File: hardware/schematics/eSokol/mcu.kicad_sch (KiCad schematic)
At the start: 14 parts, among them J1 DB25, Q6 AO3400A, SW1 SW_LITTLE, U2 YAAJ_BluePill_SWD_Breakout, U3 TP4056, U5 AMS1117-5.0, U9 TCRT5000

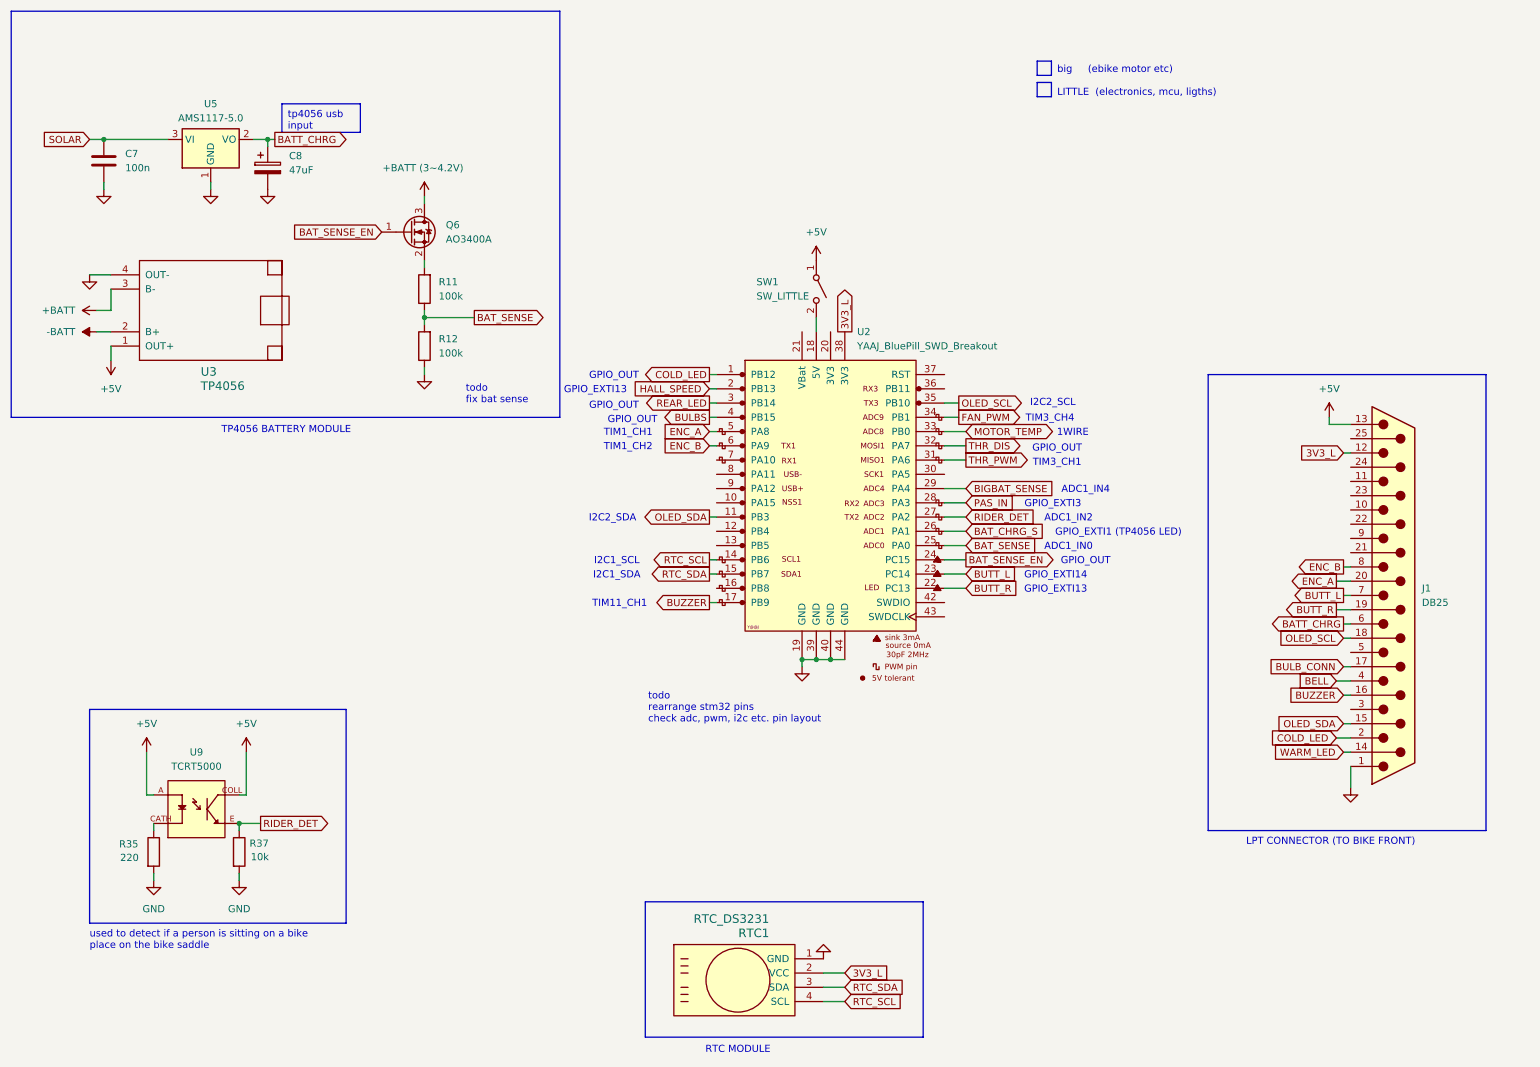
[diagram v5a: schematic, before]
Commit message: Minor lights fixes and improvements, added decoupling cap to mcu 5V, removed unused files
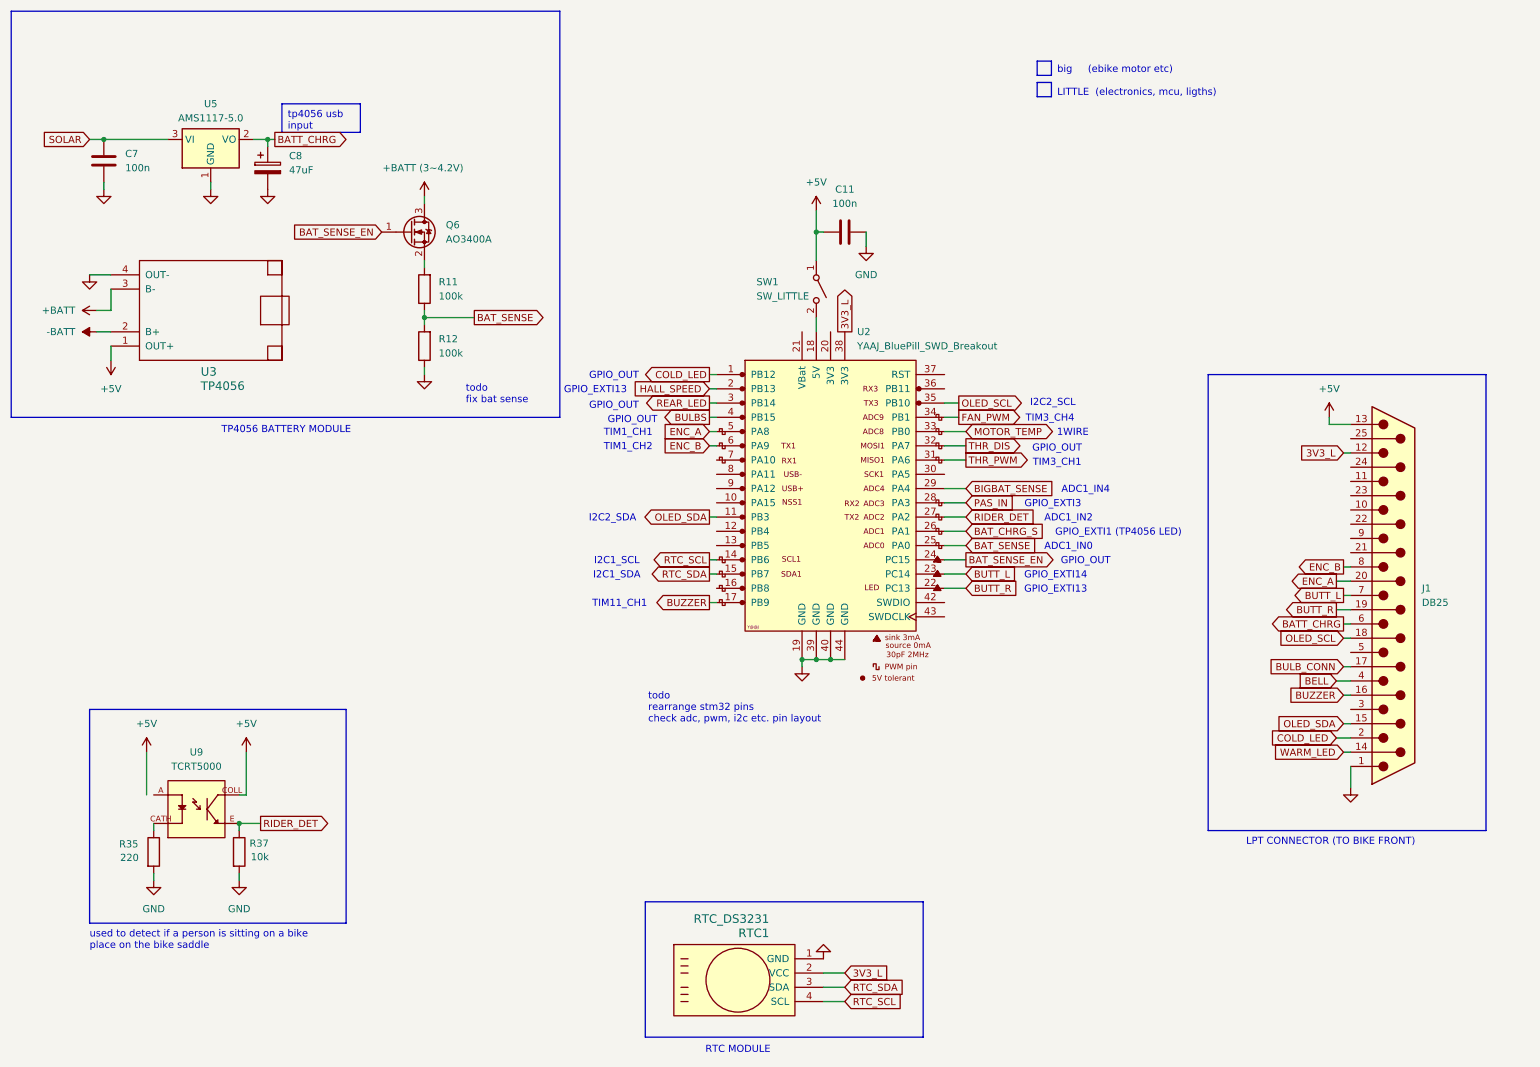
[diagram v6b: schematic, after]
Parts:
- added C11: 100n, symbol Device:C
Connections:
- net +5V: now also C11.1; no longer U9.A
- net GND: now also C11.2
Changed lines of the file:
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@@
 	)
 	(junction
+		(at 154.94 50.8)
+		(diameter 0)
+		(color 0 0 0 0)
+	)
+	(junction
 		(at 157.48 127)
 		(diameter 0)
@@
 	(wire
 		(pts
+			(xy 163.83 53.34) (xy 163.83 50.8)
+		)
+		(stroke
+			(width 0)
+			(type default)
+		)
+	)
+	(wire
+		(pts
 			(xy 46.99 41.91) (xy 46.99 43.18)
 		)
@@
 	(wire
 		(pts
+			(xy 154.94 50.8) (xy 154.94 55.88)
+		)
+		(stroke
+			(width 0)
+			(type default)
+		)
+	)
+	(wire
+		(pts
 			(xy 250.19 120.65) (xy 248.92 120.65)
 		)
@@
 	(wire
 		(pts
+			(xy 154.94 50.8) (xy 156.21 50.8)
+		)
+		(stroke
+			(width 0)
+			(type default)
+		)
+	)
+	(wire
+		(pts
 			(xy 26.67 68.58) (xy 29.21 68.58)
 		)
@@
 	(wire
 		(pts
-			(xy 35.56 151.13) (xy 36.83 151.13)
+			(xy 154.94 46.99) (xy 154.94 50.8)
 		)
 		(stroke
@@
 	)
 	(symbol
+		(lib_id "power:GND")
+		(at 163.83 53.34 0)
+		(unit 1)
+		(exclude_from_sim no)
+		(in_bom yes)
+		(on_board yes)
+		(dnp no)
+		(fields_autoplaced yes)
+		(property "Reference" "#PWR018"
+			(at 163.83 59.69 0)
+			(effects
+				(font
+					(size 1.27 1.27)
+				)
+				(hide yes)
+			)
+		)
+		(property "Value" "GND"
+			(at 163.83 58.42 0)
+			(effects
+				(font
+					(size 1.27 1.27)
+				)
+			)
+		)
+		(property "Footprint" ""
+			(at 163.83 53.34 0)
+			(effects
+				(font
+					(size 1.27 1.27)
+				)
+				(hide yes)
+			)
+		)
+		(property "Datasheet" ""
+			(at 163.83 53.34 0)
+			(effects
+				(font
+					(size 1.27 1.27)
+				)
+				(hide yes)
+			)
+		)
+		(property "Description" "Power symbol creates a global label with name \"GND\" , ground"
+			(at 163.83 53.34 0)
+			(effects
+				(font
+					(size 1.27 1.27)
+				)
+				(hide yes)
+			)
+		)
+		(pin "1"
+		)
+		(instances
+			(project ""
+				(path "/44b9e6ec-08e4-4361-b4b8-e7c9cf0a26a7/f565501d-a817-4ef9-831d-033eb352bbe6"
+					(reference "#PWR018")
+					(unit 1)
+				)
+			)
+		)
+	)
+	(symbol
 		(lib_id "power:-BATT")
 		(at 26.67 68.58 90)
@@
 	(symbol
 		(lib_id "power:+5V")
-		(at 154.94 55.88 0)
+		(at 154.94 46.99 0)
 		(unit 1)
 		(exclude_from_sim no)
@@
 		(fields_autoplaced yes)
 		(property "Reference" "#PWR016"
-			(at 154.94 59.69 0)
+			(at 154.94 50.8 0)
 			(effects
 				(font
@@
 		)
 		(property "Value" "+5V"
-			(at 154.94 50.8 0)
+			(at 154.94 41.91 0)
 			(effects
 				(font
@@
 		)
 		(property "Footprint" ""
-			(at 154.94 55.88 0)
+			(at 154.94 46.99 0)
 			(effects
 				(font
@@
 		)
 		(property "Datasheet" ""
-			(at 154.94 55.88 0)
+			(at 154.94 46.99 0)
 			(effects
 				(font
@@
 		)
 		(property "Description" "Power symbol creates a global label with name \"+5V\""
-			(at 154.94 55.88 0)
+			(at 154.94 46.99 0)
 			(effects
 				(font
@@
 					(unit 1)
 				)
+			)
+		)
+	)
+	(symbol
+		(lib_id "Device:C")
+		(at 160.02 50.8 90)
+		(unit 1)
+		(exclude_from_sim no)
+		(in_bom yes)
+		(on_board yes)
+		(dnp no)
+		(fields_autoplaced yes)
+		(property "Reference" "C11"
+			(at 160.02 43.18 90)
+			(effects
+				(font
+					(size 1.27 1.27)
+				)
+			)
+		)
+		(property "Value" "100n"
+			(at 160.02 45.72 90)
+			(effects
+				(font
+					(size 1.27 1.27)
+				)
+			)
+		)
+		(property "Footprint" ""
+			(at 163.83 49.8348 0)
+			(effects
+				(font
+					(size 1.27 1.27)
+				)
+				(hide yes)
+			)
+		)
+		(property "Datasheet" "~"
+			(at 160.02 50.8 0)
+			(effects
+				(font
+					(size 1.27 1.27)
+				)
+				(hide yes)
+			)
+		)
+		(property "Description" "Unpolarized capacitor"
+			(at 160.02 50.8 0)
+			(effects
+				(font
+					(size 1.27 1.27)
+				)
+				(hide yes)
+			)
+		)
+		(pin "2"
+		)
+		(pin "1"
+		)
+		(instances
+			(project ""
+				(path "/44b9e6ec-08e4-4361-b4b8-e7c9cf0a26a7/f565501d-a817-4ef9-831d-033eb352bbe6"
+					(reference "C11")
+					(unit 1)
+				)

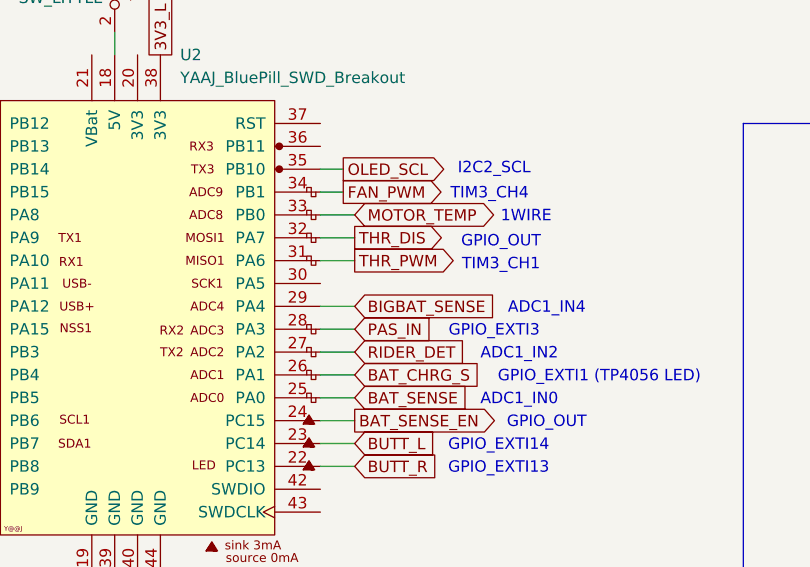
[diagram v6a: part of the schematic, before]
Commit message: schematics: eSokol: big: replace SW_SPORT with digital THR_SPORT input
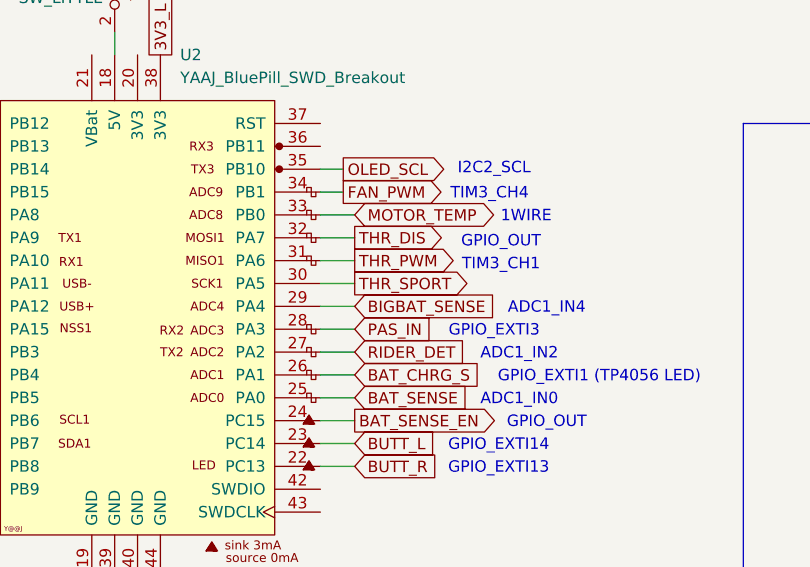
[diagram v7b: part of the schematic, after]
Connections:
- net THR_SPORT: now reaches U2.30 (PA5)
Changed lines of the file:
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@@
 	(wire
 		(pts
+			(xy 177.8 93.98) (xy 181.61 93.98)
+		)
+		(stroke
+			(width 0)
+			(type default)
+		)
+	)
+	(wire
+		(pts
 			(xy 246.38 85.09) (xy 250.19 85.09)
 		)
@@
 		)
 	)
+	(global_label "THR_SPORT"
+		(shape output)
+		(at 181.61 93.98 0)
+		(fields_autoplaced yes)
+		(effects
+			(font
+				(size 1.27 1.27)
+				(color 204 102 0 1)
+			)
+			(justify left)
+		)
+		(property "Intersheetrefs" "${INTERSHEET_REFS}"
+			(at 195.1785 93.98 0)
+			(effects
+				(font
+					(size 1.27 1.27)
+				)
+				(justify left)
+				(hide yes)
+			)
+		)
+	)
 	(global_label "BAT_SENSE"
 		(shape output)
@@
 	)
 	(symbol
-		(lib_id "Device:C")
-		(at 160.02 50.8 90)
+		(lib_id "Device:R")
+		(at 36.83 161.29 0)
 		(unit 1)
 		(exclude_from_sim no)
@@
 		(on_board yes)
 		(dnp no)
-		(fields_autoplaced yes)
-		(property "Reference" "C11"
-			(at 160.02 43.18 90)
+		(property "Reference" "R35"
+			(at 32.385 159.893 0)
 			(effects
 				(font
@@
 			)
 		)
-		(property "Value" "100n"
-			(at 160.02 45.72 90)
+		(property "Value" "220"
+			(at 32.512 162.306 0)
 			(effects
 				(font
@@
 		)
 		(property "Footprint" ""
-			(at 163.83 49.8348 0)
+			(at 35.052 161.29 90)
 			(effects
 				(font
@@
 		)
 		(property "Datasheet" "~"
-			(at 160.02 50.8 0)
+			(at 36.83 161.29 0)
 			(effects
 				(font
@@
 			)
 		)
-		(property "Description" "Unpolarized capacitor"
-			(at 160.02 50.8 0)
+		(property "Description" "Resistor"
+			(at 36.83 161.29 0)
 			(effects
 				(font
@@
 			)
 		)
-		(pin "2"
-		)
 		(pin "1"
 		)
+		(pin "2"
+		)
 		(instances
 			(project ""
 				(path "/44b9e6ec-08e4-4361-b4b8-e7c9cf0a26a7/f565501d-a817-4ef9-831d-033eb352bbe6"
-					(reference "C11")
+					(reference "R35")
 					(unit 1)
 				)
@@
 	)
 	(symbol
-		(lib_id "Device:R")
-		(at 36.83 161.29 0)
+		(lib_id "Device:C")
+		(at 160.02 50.8 90)
 		(unit 1)
 		(exclude_from_sim no)
@@
 		(on_board yes)
 		(dnp no)
-		(property "Reference" "R35"
-			(at 32.385 159.893 0)
+		(fields_autoplaced yes)
+		(property "Reference" "C11"
+			(at 160.02 43.18 90)
 			(effects
 				(font
@@
 			)
 		)
-		(property "Value" "220"
-			(at 32.512 162.306 0)
+		(property "Value" "100n"
+			(at 160.02 45.72 90)
 			(effects
 				(font
@@
 		)
 		(property "Footprint" ""
-			(at 35.052 161.29 90)
+			(at 163.83 49.8348 0)
 			(effects
 				(font
@@
 		)
 		(property "Datasheet" "~"
-			(at 36.83 161.29 0)
+			(at 160.02 50.8 0)
 			(effects
 				(font
@@
 			)
 		)
-		(property "Description" "Resistor"
-			(at 36.83 161.29 0)
+		(property "Description" "Unpolarized capacitor"
+			(at 160.02 50.8 0)
 			(effects
 				(font
@@
 			)
 		)
-		(pin "1"
-		)
 		(pin "2"
 		)
+		(pin "1"
+		)
 		(instances
 			(project ""
 				(path "/44b9e6ec-08e4-4361-b4b8-e7c9cf0a26a7/f565501d-a817-4ef9-831d-033eb352bbe6"
-					(reference "R35")
+					(reference "C11")
 					(unit 1)
 				)
